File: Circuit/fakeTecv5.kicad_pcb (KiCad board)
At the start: 2 copper layers, 25.4 x 52.1 mm, 36 parts, among them J11 T1 3,3, J12 T2 3,3, J13 T3 3,3, J14 GPS Pins, J16 Encoder Pins, J5 I2C Oled screen, J6 FET1 Drain, J7 FET2 Drain, J8 FET3 Drain, J9 Battery Connector, Q1 AO3400A, Q2 AO3400A, Q3 AO3400A, SW1 Reset, SW2 SW_Push, U1 XB8089D0, U2 HT-RA62, U3 nice!nano v2

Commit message: Added pull up resistors and ground pad to rotary encoder pads
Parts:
- removed JP1: ~, Jumper:SolderJumper-3_P1.3mm_Open_RoundedPad1.0x1.5mm
- added R10: 10k, Resistor_SMD:R_0805_2012Metric_Pad1.20x1.40mm_HandSolder, B.Cu at (113.5, 48.5)
- added R11: 10k, Resistor_SMD:R_0805_2012Metric_Pad1.20x1.40mm_HandSolder, B.Cu at (111.6, 48.5)
- added R9: 10k, Resistor_SMD:R_0805_2012Metric_Pad1.20x1.40mm_HandSolder, B.Cu at (115.4, 48.5)
- J11: value T1 3,3 -> FET1 3,3; footprint SMD_PAD:SMD_PAD_1x1 -> SMD_PAD:SMD_PAD_1x01
- J12: value T2 3,3 -> FET2 3,3; footprint SMD_PAD:SMD_PAD_1x1 -> SMD_PAD:SMD_PAD_1x01
- J13: value T3 3,3 -> FET3 3,3; footprint SMD_PAD:SMD_PAD_1x1 -> SMD_PAD:SMD_PAD_1x01
- J14: footprint SMD_PAD:SMD_PAD_4x1 -> SMD_PAD:SMD_PAD_1x04
- J16: value Encoder Pins -> Encoder Pads; footprint SMD_PAD:SMD_PAD_3x1 -> SMD_PAD:SMD_PAD_1x04
- J6, J7, J8: footprint SMD_PAD:SMD_PAD_1x1 -> SMD_PAD:SMD_PAD_1x01
- moved C1 12.0 mm to (104.4, 48.3), turned to 0 degrees
- moved R5 9.04 mm to (104.4, 50.3), turned to 0 degrees
- moved R4 8.13 mm to (102.4, 52.2), turned to 180 degrees
- moved J16 2.27 mm to (107.3, 53.5), turned to 0 degrees
- turned J14 to 0 degrees
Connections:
- J16 pad 1: Net-(J16-Pin_1) -> GND
- J16 pad 2: Net-(J16-Pin_2) -> /ENC_PUSH
- J16 pad 3: Net-(J16-Pin_3) -> /ENC_B
- J6 pad 1: Net-(J6-Pin_1) -> /GPS_GND
- Q1 pad 3: Net-(JP1-C) -> /GPS_GND
- U3 pad 24: /NBat+ -> +BATT
- U3 pad 25: /NBat+ -> +BATT
- U3 pad 26: Net-(J16-Pin_3) -> /ENC_A
- U3 pad 27: Net-(J16-Pin_2) -> /ENC_B
- U3 pad 28: Net-(J16-Pin_1) -> /ENC_PUSH
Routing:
- net /SCK: track 26.0 -> 47.4 mm, vias 2 -> 0
- net /Batt%: track 29.9 -> 18.6 mm
- net /ENC_A: track 0.00 -> 6.70 mm, vias 0 -> 1
- net /ENC_PUSH: track 0.00 -> 6.66 mm, vias 0 -> 1
- net /ENC_B: track 0.00 -> 6.45 mm, vias 0 -> 1
- net +3.3V: track 94.0 -> 99.7 mm, vias 1 -> 2
- net /FET1: track 5.60 -> 10.7 mm
- net /GPS_GND: track 3.10 -> 8.22 mm
- net Net-(J16-Pin_3): track 4.84 -> 0.00 mm, vias 1 -> 0
- net Net-(J16-Pin_1): track 4.58 -> 0.00 mm, vias 1 -> 0
- net Net-(J16-Pin_2): track 4.53 -> 0.00 mm, vias 1 -> 0
- net Net-(JP1-C): track 3.53 -> 0.00 mm
- net Net-(J6-Pin_1): track 2.84 -> 0.00 mm
- net +BATT: track 72.8 -> 74.1 mm
- net /BUSY: track 32.5 -> 33.3 mm
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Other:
- board text added: "<ENC"
- board text added: "<GPS"
- board text added: "OLED < Screen"
- board text added: "RX"
- board text added: "TX"
- board text added: "fakeTec custom By Jacob"
- board text removed: "D10"
- board text removed: "D14"
- board text removed: "D15"
- board text removed: "D16"
- board text removed: "D18"
- board text removed: "D19"
- board text removed: "D2"
- board text removed: "D20"
- board text removed: "D21"
- board text removed: "D3"
- board text removed: "D4"
- board text removed: "D5"
- board text removed: "D6"
- board text removed: "D7"
- board text removed: "D8"
- board text removed: "D9"
- board text removed: "ENC:"
- board text removed: "GPS:"
- board text removed: "GPS>"
- board text removed: "OLED Screen"
- board text removed: "TXEN"
- board text removed: "fakeTec G@W By Jacob Lucas"
- board text removed: "to RX"
- board text removed: "to TX"

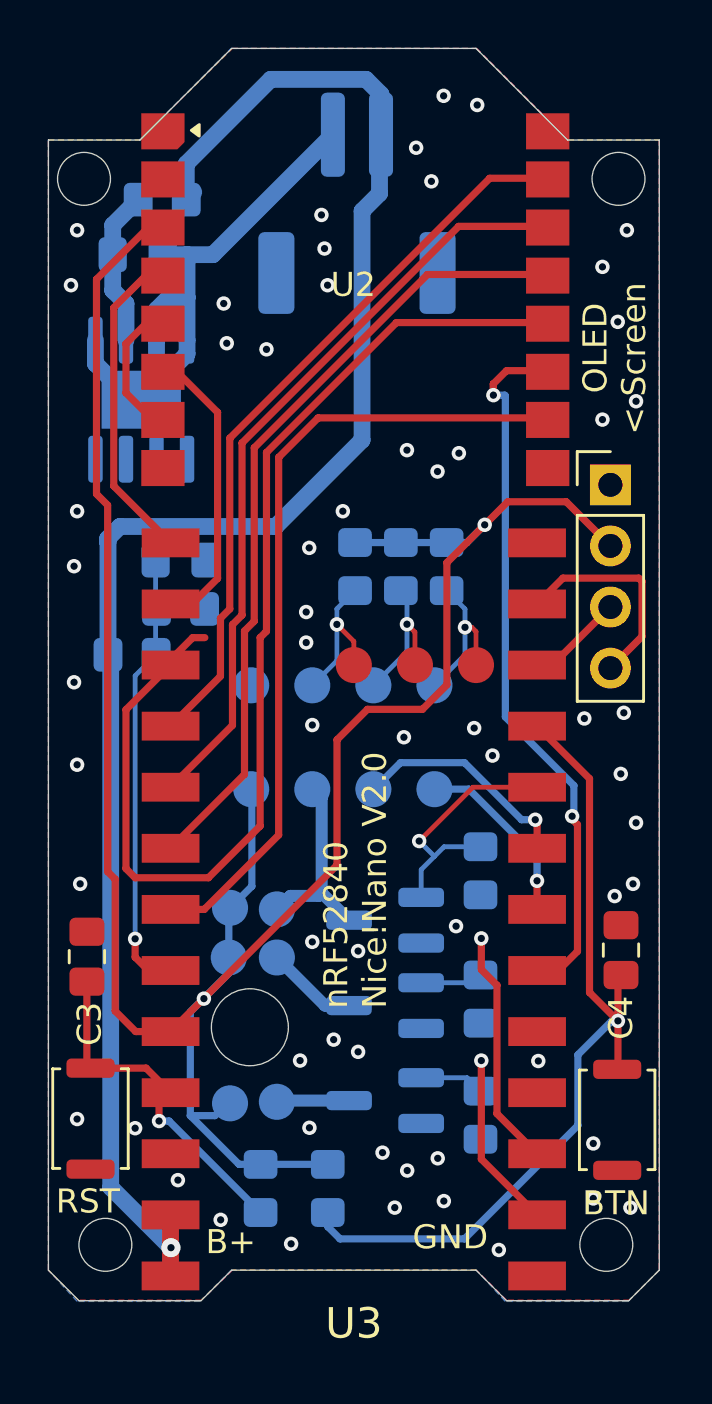
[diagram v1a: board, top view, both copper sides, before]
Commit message: renamed to rotTec and pcb artwork updated
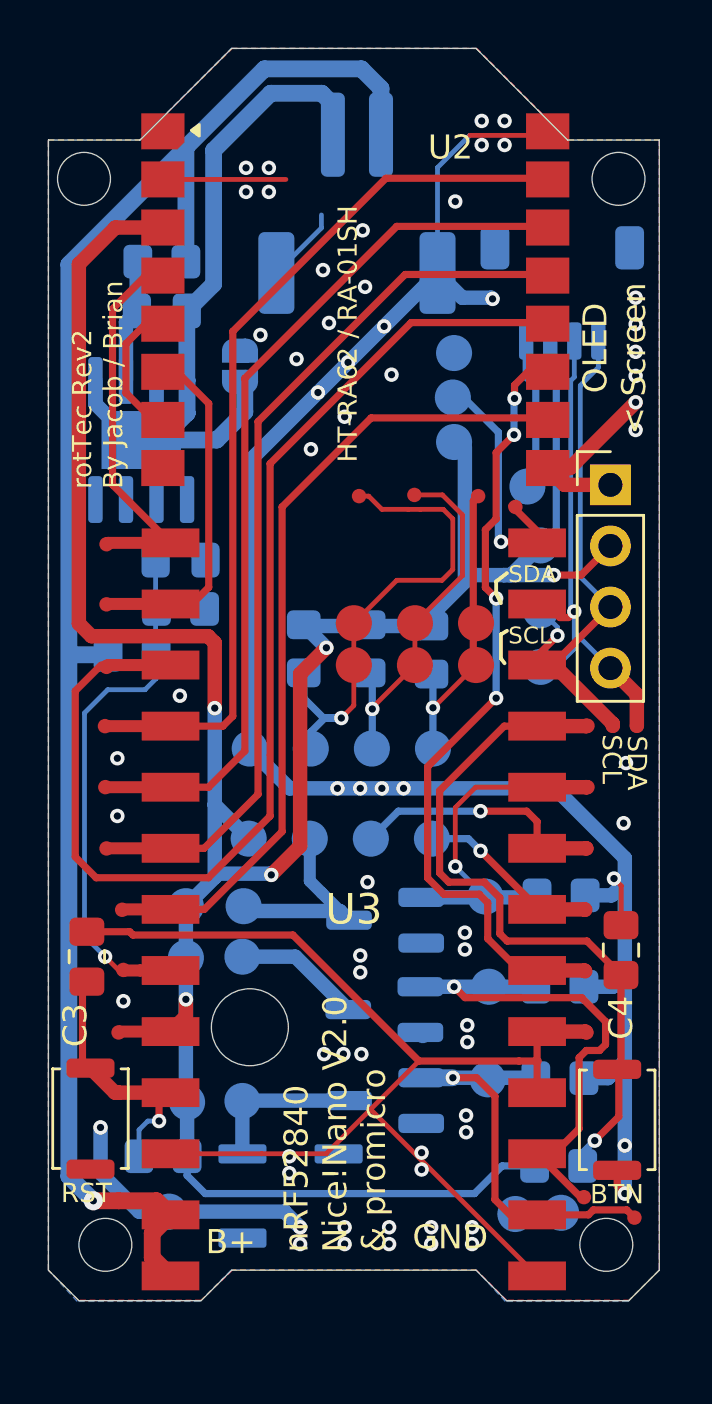
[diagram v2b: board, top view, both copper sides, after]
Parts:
- added BZ1: Buzzer, faketec:Buzzer_5020, B.Cu at (109.0, 74.7)
- added J1: EXTRA, faketec:SMD_PAD_1x01, B.Cu at (115.7, 41.5)
- added J10: ~, faketec:TestPoint_Pad_Slim_D0.6mm, F.Cu at (101.3, 50.1)
- added J15: ~, faketec:TestPoint_Pad_Slim_D0.6mm, F.Cu at (101.3, 52.7)
- added J17: ~, faketec:TestPoint_Pad_Slim_D0.6mm, F.Cu at (101.2, 55.2)
- added J18: ~, faketec:TestPoint_Pad_Slim_D0.6mm, F.Cu at (101.2, 57.7)
- added J19: ~, faketec:TestPoint_Pad_Slim_D0.6mm, F.Cu at (101.3, 60.2)
- added J2: ~, faketec:TestPoint_Pad_Slim_D0.6mm, F.Cu at (114.1, 45.5)
- added J20: ~, faketec:TestPoint_Pad_Slim_D0.6mm, F.Cu at (102.0, 62.8)
- added J21: ~, faketec:TestPoint_Pad_Slim_D0.6mm, F.Cu at (102.0, 65.3)
- added J22: ~, faketec:TestPoint_Pad_Slim_D0.6mm, F.Cu at (116.8, 45.6)
- added J23: ~, faketec:TestPoint_Pad_Slim_D0.6mm, F.Cu at (118.3, 46.0)
- added J24: ~, faketec:TestPoint_Pad_Slim_D0.6mm, F.Cu at (123.3, 55.1)
- added J25: ~, faketec:TestPoint_Pad_Slim_D0.6mm, F.Cu at (122.3, 55.1)
- added J26: ~, faketec:TestPoint_Pad_Slim_D0.6mm, F.Cu at (121.2, 55.1)
- added J27: ~, faketec:TestPoint_Pad_Slim_D0.6mm, F.Cu at (121.2, 57.7)
- added J28: ~, faketec:TestPoint_Pad_Slim_D0.6mm, F.Cu at (121.2, 60.2)
- added J29: ~, faketec:TestPoint_Pad_Slim_D0.6mm, F.Cu at (121.2, 62.8)
- added J3: ~, faketec:TestPoint_Pad_Slim_D0.6mm, F.Cu at (111.8, 45.6)
- added J30: ~, faketec:TestPoint_Pad_Slim_D0.6mm, F.Cu at (121.2, 65.3)
- added J31: ~, faketec:TestPoint_Pad_Slim_D0.6mm, F.Cu at (121.2, 74.8)
- added J32: ~, faketec:TestPoint_Pad_Slim_D0.6mm, F.Cu at (123.2, 75.6)
- added J33: ~, faketec:TestPoint_Pad_Slim_D0.6mm, F.Cu at (121.2, 67.9)
- added J34: ~, faketec:TestPoint_Pad_Slim_D0.6mm, F.Cu at (101.8, 74.9)
- added J35: ~, faketec:TestPoint_Pad_Slim_D0.6mm, F.Cu at (101.8, 67.9)
- added J36: ~, faketec:TestPoint_Pad_Slim_D0.6mm, F.Cu at (101.8, 70.4)
- added J37: SCL, faketec:SMD_PAD_1x01, B.Cu at (119.3, 50.4)
- added J38: QWIIC, Connector_JST:JST_SH_SM04B-SRSS-TB_1x04-1MP_P1.00mm_Horizontal, B.Cu at (120.2, 37.1)
- added J39: SDA, faketec:SMD_PAD_1x01, B.Cu at (119.3, 52.7)
- added J4: ~, faketec:TestPoint_Pad_Slim_D0.6mm, F.Cu at (101.3, 47.6)
- added J40: 3.3V, faketec:SMD_PAD_1x01, B.Cu at (119.3, 47.6)
- added J41: GND, faketec:SMD_PAD_1x01, B.Cu at (118.8, 45.2)
- added J42: FET1, faketec:SMD_PAD_1x01, B.Cu at (117.0, 62.2)
- added J43: FET2, faketec:SMD_PAD_1x01, B.Cu at (117.2, 66.0)
- added J44: FET3, faketec:SMD_PAD_1x01, B.Cu at (117.2, 69.8)
- added J45: GND, faketec:SMD_PAD_1x01, B.Cu at (115.8, 39.6)
- added J46: 3.3V, faketec:SMD_PAD_1x01, B.Cu at (115.8, 43.4)
- added J47: GND, faketec:SMD_PAD_1x01, B.Cu at (120.2, 75.4)
- added J48: GND, faketec:SMD_PAD_1x01, B.Cu at (118.3, 75.5)
- added J49: GND, faketec:SMD_PAD_1x01, B.Cu at (103.9, 75.3)
- added JP1: Jumper_2_Open, Jumper:SolderJumper-2_P1.3mm_Open_RoundedPad1.0x1.5mm, B.Cu at (106.8, 40.2)
- J11, J12, J13, J6, J7, J8: footprint SMD_PAD:SMD_PAD_1x01 -> faketec:SMD_PAD_1x01
- J14, J16: footprint SMD_PAD:SMD_PAD_1x04 -> faketec:SMD_PAD_1x04
- U2: footprint HeltecModule:HT-RA62 -> faketec:HT-RA62
- U3: footprint N!ce_Nano:NICE!NANO V2_2 SMD -> faketec:NICE!NANO and pro-micro V2_2 SMD
- moved R7 9.65 mm to (120.1, 73.5), turned to 180 degrees
- moved R8 4.27 mm to (103.7, 73.0), turned to 180 degrees
- moved R11 4.03 mm to (109.5, 52.0)
- moved R10 3.67 mm to (112.2, 52.0)
- moved R3 3.64 mm to (120.2, 69.8), turned to 180 degrees
- moved R9 3.53 mm to (114.8, 52.0)
- moved R1 3.50 mm to (120.2, 62.2), turned to 180 degrees
- moved R2 3.34 mm to (120.2, 66.0), turned to 180 degrees
- moved J16 2.63 mm to (107.3, 56.1)
- moved R6 2.58 mm to (103.6, 35.9)
- moved C2 2.55 mm to (103.6, 37.9)
- moved J14 2.06 mm to (107.2, 59.8)
- moved J11 1.84 mm to (104.6, 62.6)
- moved J13 1.79 mm to (104.7, 70.8)
- moved J12 1.78 mm to (104.6, 64.8)
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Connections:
- net Net-(J14-Pin_3) renamed /GPSRX
- net Net-(J14-Pin_4) renamed /GPSTX
- net Net-(J8-Pin_1) renamed /BUZZER
- U3 pad 12: unconnected-(U3-P1.06-Pad12) -> /EXTRA
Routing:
- net GND: track 0.00 -> 156.9 mm, vias 61 -> 68
- net +3.3V: track 99.7 -> 119.2 mm, vias 2 -> 5
- net /SCL: track 4.05 -> 23.1 mm, vias 0 -> 1
- net /ENC_PUSH: track 6.66 -> 20.7 mm
- net /SDA: track 9.46 -> 21.8 mm, vias 0 -> 1
- net -BATT: track 25.0 -> 34.2 mm
- net /EXTRA: track 0.00 -> 9.20 mm, vias 0 -> 1
- net /FET3: track 11.4 -> 20.2 mm
- net /ENC_B: track 6.45 -> 15.2 mm
- net /ENC_A: track 6.70 -> 14.7 mm
- net /FET2: track 14.1 -> 21.8 mm
- net /Batt%: track 18.6 -> 25.3 mm
- net /CS: track 31.2 -> 37.8 mm
- net /BTN: track 36.0 -> 29.7 mm
- net /MOSI: track 31.9 -> 37.1 mm
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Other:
- board text added: "100nF"
- board text added: "10KΩ"
- board text added: "1KΩ"
- board text added: "1MΩ"
- board text added: "3.3V"
- board text added: "5020> Buzzer"
- board text added: "680Ω"
- board text added: "BLE ANTENNA"
- board text added: "Bypass > XB8089D0"
- board text added: "HT-RA62 / RA-01SH"
- board text added: "I2C"
- board text added: "P0.06 ( 6)"
- board text added: "P0.08 ( 8)"
- board text added: "P0.24 (24)"
- board text added: "P1.06(38)"
- board text added: "Qx: N-CHN MOSFET AO3400A"
- board text added: "buz"
- board text added: "gps"
- board text added: "nRF52840 Nice!Nano V2.0 & promicro"
- board text added: "rotTec Rev2 By Jacob / Brian"
- board text added: "vib"
- board text removed: "3,3"
- board text removed: "3.3"
- board text removed: "fakeTec custom By Jacob"
- board text removed: "nRF52840 Nice!Nano V2.0"
- board text removed: "|"

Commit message: Rename from rotTec_pcb to roTec and pdf and clean up schematic and pcb
Also add 3D printed case with fixed usb Type-C port position
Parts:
- SW1, SW2: footprint Button_Switch_SMD:SW_Push_SPST_NO_Alps_SKRK -> faketec:SW_Push_SPST_NO_Alps_SKRK
- moved R4 2.46 mm to (101.0, 50.1), turned to 90 degrees
- moved C1 1.91 mm to (104.8, 50.1), turned to 90 degrees
- moved R5 1.48 mm to (102.9, 50.1), turned to 90 degrees
- moved J38 0.80 mm to (120.2, 38.0)
- moved U1 0.67 mm to (102.7, 42.6)
- moved JP1 0.35 mm to (106.9, 40.5)
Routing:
- net GND: track 156.9 -> 225.8 mm, vias 68 -> 70
- net /Batt%: track 25.3 -> 24.3 mm
- net /SDA: track 21.8 -> 21.0 mm
- net /SCL: track 23.1 -> 22.3 mm
- net +3.3V: track 119.2 -> 118.4 mm
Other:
- board text added: "< Battery BMS Bypass"
- board text added: "Rx and Cx are 0805 Sized"
- board text added: "XB8089D0"
- board text added: "roTec Rev3 By Jacob / Brian"
- board text removed: "Bypass > XB8089D0"
- board text removed: "rotTec Rev2 By Jacob / Brian"

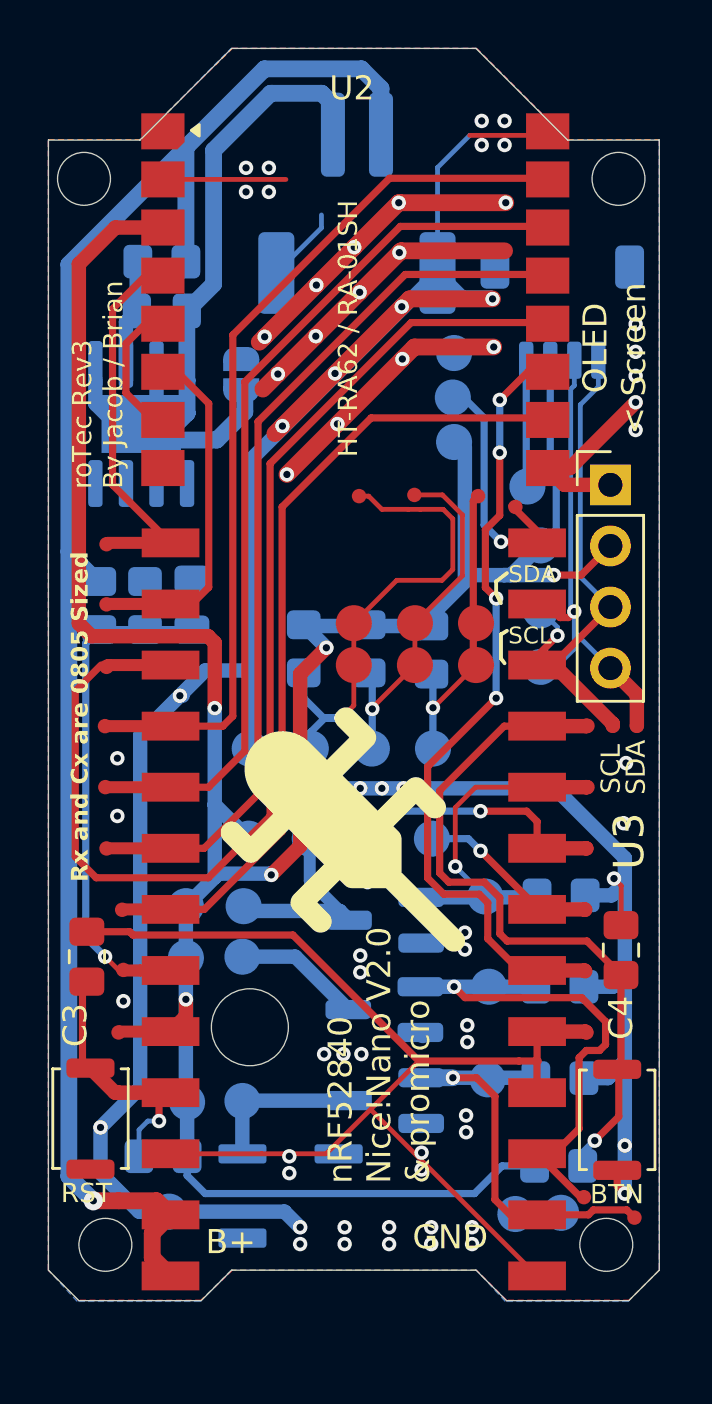
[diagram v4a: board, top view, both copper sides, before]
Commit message: Removed resistor and capacitor for button and also add integrated test pads.
Also added jlcpcb design rules
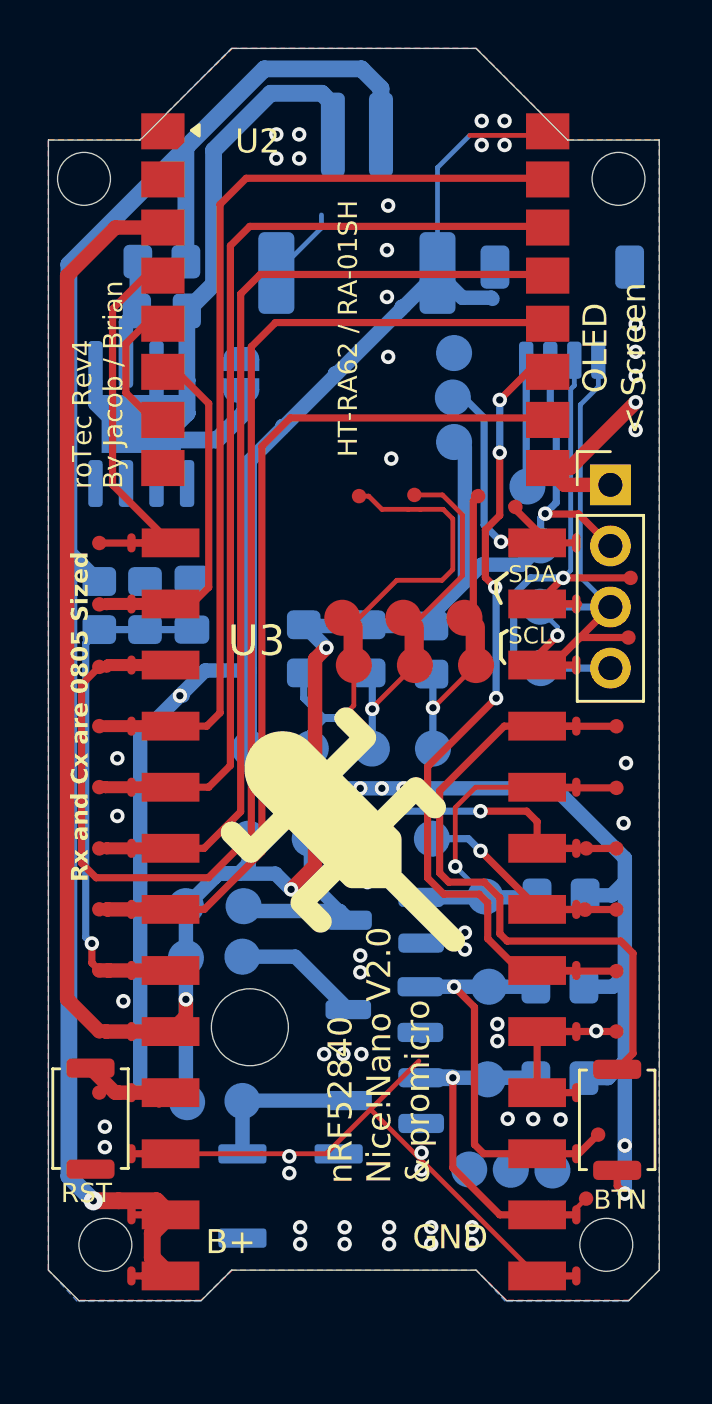
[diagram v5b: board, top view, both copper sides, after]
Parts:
- removed C3, C4: 100nF, Capacitor_SMD:C_0805_2012Metric_Pad1.18x1.45mm_HandSolder
- removed R7, R8: 10k, Resistor_SMD:R_0805_2012Metric_Pad1.20x1.40mm_HandSolder
- BZ1: value Buzzer -> Buzzer 5020
- J38: value QWIIC -> JST-SH-4
- J9: value Battery Connector -> JST-PH-2
- R5: value 1M -> 1.0M
- moved J49 16.0 mm to (119.8, 73.6)
- moved J24 6.16 mm to (123.1, 49.0)
- moved J25 3.73 mm to (123.0, 51.5)
- moved J47 2.75 mm to (118.1, 73.6)
- moved J48 2.67 mm to (116.4, 73.6)
- moved J31 2.67 mm to (121.7, 72.2)
- moved J32 2.16 mm to (121.2, 74.8)
- moved J29 1.30 mm to (122.5, 62.8)
- moved J30 1.30 mm to (122.5, 65.3)
- moved J33 1.25 mm to (122.5, 67.9)
- moved J27 1.25 mm to (122.5, 57.7)
- moved J26 1.25 mm to (122.5, 55.2)
- moved J28 1.25 mm to (122.5, 60.2)
- moved J21 1.00 mm to (101.0, 65.3)
- moved J20 0.95 mm to (101.0, 62.8)
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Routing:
- net GND: track 225.8 -> 137.8 mm, vias 70 -> 60
- net +3.3V: track 118.4 -> 100.9 mm, vias 5 -> 4
- net /RST_BTN: track 10.8 -> 4.43 mm, vias 1 -> 0
- net /FET2: track 21.8 -> 15.6 mm
- net /SDA: track 21.0 -> 25.4 mm
- net /FET3: track 20.2 -> 16.3 mm
- net /MOSI: track 37.0 -> 40.7 mm
- net /MISO: track 37.2 -> 40.8 mm
- net /CS: track 37.7 -> 40.8 mm
- net /SCK: track 49.4 -> 52.5 mm
- net /SCL: track 22.3 -> 25.2 mm
- net /BUSY: track 34.0 -> 36.6 mm
- net /BTN: track 29.7 -> 27.4 mm, vias 1 -> 0
- net /Batt%: track 24.3 -> 22.2 mm
- net /GPSTX: track 7.64 -> 8.96 mm
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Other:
- board text added: "roTec Rev4 By Jacob / Brian"
- board text removed: "roTec Rev3 By Jacob / Brian"

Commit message: bom update and added extra power pads for easier adjustments
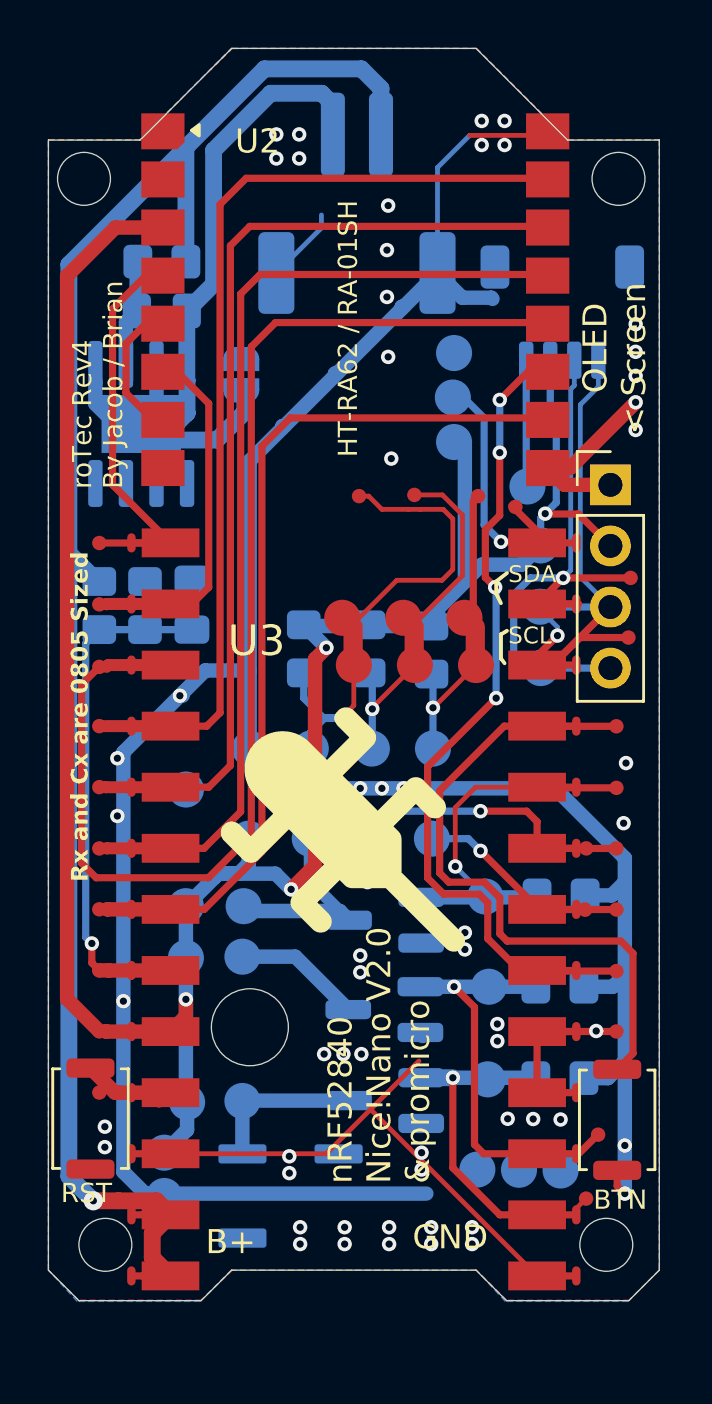
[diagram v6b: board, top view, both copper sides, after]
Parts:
- added J50: 3.3V, faketec:SMD_PAD_1x01, B.Cu at (103.7, 72.9)
- added J51: GND, faketec:SMD_PAD_1x01, B.Cu at (104.6, 57.8)
- added J52: GND, faketec:SMD_PAD_1x01, B.Cu at (103.7, 74.7)
- moved J47 0.34 mm to (118.5, 73.6)
- moved J48 0.34 mm to (116.7, 73.6)
- moved J49 0.34 mm to (120.2, 73.6)
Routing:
- net GND: track 137.8 -> 154.5 mm
- net +3.3V: track 100.9 -> 103.4 mm
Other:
- board text added: "<GND"
